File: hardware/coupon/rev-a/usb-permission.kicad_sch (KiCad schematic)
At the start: 31 parts, among them U10 SN74LVC1G00DBVR, U11 SN74LVC1G04DBVR, U12 SN74LVC1G04DBVR, U13 SN74LVC1G04DBVR, U14 SN74LVC1G04DBVR, U15 SN74LVC1G08DBVR, U16 SN74LVC1G32DBVR, U17 SN74LVC1G11DBVR, U18 SN74LVC1G08DBVR, U19 SN74LVC1G11DBVR, U20 SN74LVC1G11DBVR, U21 SN74LVC1G11DBVR, U22 SN74LVC1G32DBVR, U23 SN74LVC1G06DBVR

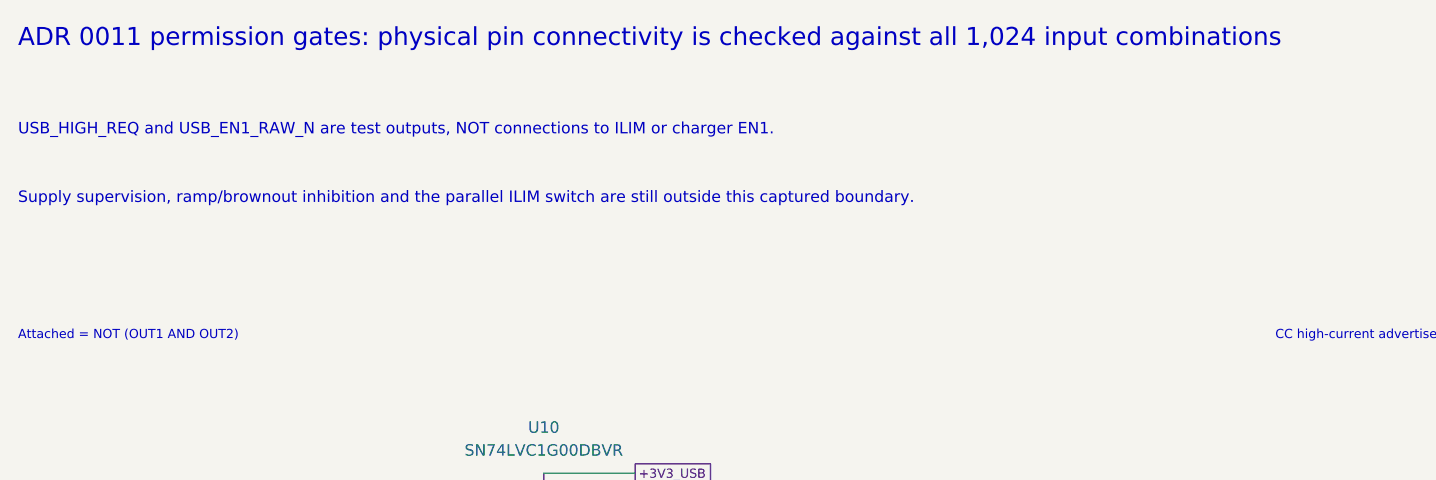
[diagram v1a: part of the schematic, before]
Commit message: Review native USB capture and add staged logic-rail supervision
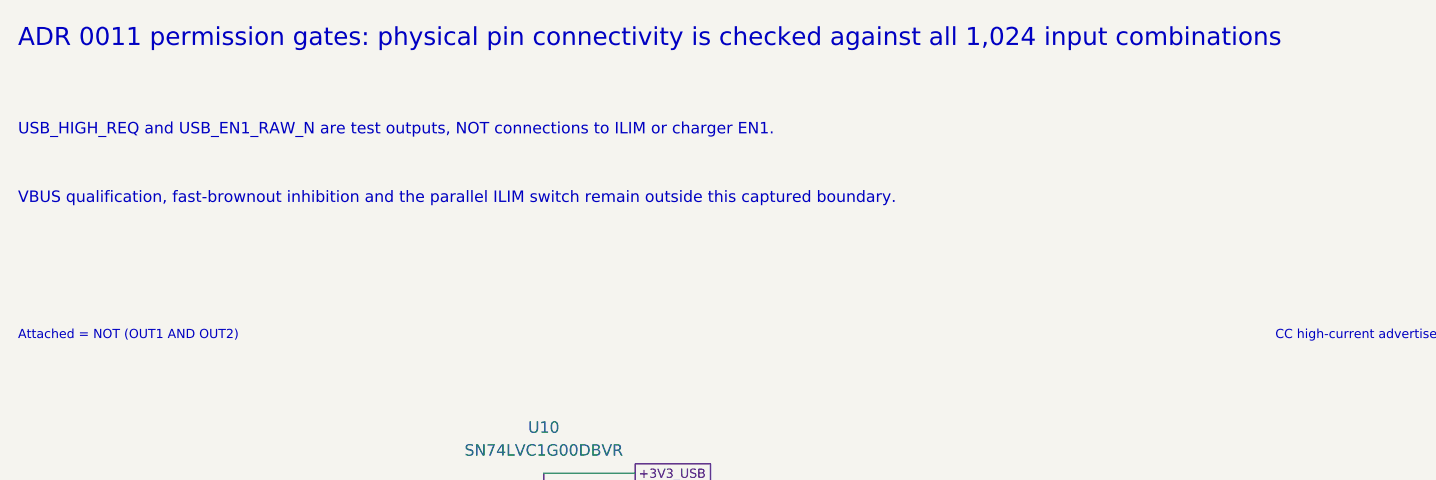
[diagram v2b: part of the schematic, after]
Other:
- note added: "VBUS qualification, fast-brownout inhibition and the parallel ILIM switch remain outside this captured boundary."
- note removed: "Supply supervision, ramp/brownout inhibition and the parallel ILIM switch are still outside this captured boundary."
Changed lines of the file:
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@@
 (text "ADR 0011 permission gates: physical pin connectivity is checked against all 1,024 input combinations" (at 20.320 20.320 0) (effects (font (size 2 2)) (justify left)))
 (text "USB_HIGH_REQ and USB_EN1_RAW_N are test outputs, NOT connections to ILIM or charger EN1." (at 20.320 30.480 0) (effects (font (size 1.27 1.27)) (justify left)))
-(text "Supply supervision, ramp/brownout inhibition and the parallel ILIM switch are still outside this captured boundary." (at 20.320 38.100 0) (effects (font (size 1.27 1.27)) (justify left)))
+(text "VBUS qualification, fast-brownout inhibition and the parallel ILIM switch remain outside this captured boundary." (at 20.320 38.100 0) (effects (font (size 1.27 1.27)) (justify left)))
 (text "Attached = NOT (OUT1 AND OUT2)" (at 20.320 53.340 0) (effects (font (size 1.016 1.016)) (justify left)))
 (symbol (lib_id "rgb-badge-coupon:SN74LVC1G00DBVR") (at 78.740 76.200 0) (unit 1)

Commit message: Simplify charging to Type-C-only fixed-current policy
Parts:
- removed C10, C12, C13, C14, C15, C16, C18, C19, C20, C21, C22: 100n 16V X7R, rgb-badge-coupon:C_Murata_GRM15_0402, symbol rgb-badge-coupon:GRM155R71C104KA88D
- removed U10: SN74LVC1G00DBVR, rgb-badge-coupon:SOT23_TI_DBV0005A, symbol rgb-badge-coupon:SN74LVC1G00DBVR
- removed U12, U13, U14: SN74LVC1G04DBVR, rgb-badge-coupon:SOT23_TI_DBV0005A, symbol rgb-badge-coupon:SN74LVC1G04DBVR
- removed U15, U18: SN74LVC1G08DBVR, rgb-badge-coupon:SOT23_TI_DBV0005A, symbol rgb-badge-coupon:SN74LVC1G08DBVR
- removed U16, U22: SN74LVC1G32DBVR, rgb-badge-coupon:SOT23_TI_DBV0005A, symbol rgb-badge-coupon:SN74LVC1G32DBVR
- removed U19, U20, U21: SN74LVC1G11DBVR, rgb-badge-coupon:SOT23_TI_DBV0006A, symbol rgb-badge-coupon:SN74LVC1G11DBVR
- TP30: value HIGH_REQ -> CHARGE_REQ
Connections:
- net USB_ATTACHED is gone; now on net USB_CC_HIGH: U17.6 (C)
- net USB_READY_ATTACHED is gone; now on net USB_CHARGE_REQ: U17.4 (Y)
- net USB_RUN_REQ is gone; now on net USB_CHARGE_REQ: U23.2 (A)
- net USB_HIGH_REQ renamed USB_CHARGE_REQ
- no-connect marks 5 -> 2
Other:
- note added: "ADR 0013: one fixed current limit; 16 stable Type-C/supply combinations checked"
- note added: "Both supplies valid AND Type-C permission"
- note added: "Open-drain request; not charger pin"
- note added: "Type-C advertises 1.5 A or 3 A"
- note added: "USB_CHARGE_REQ and USB_EN1_RAW_N are test outputs, NOT a physical charger EN1 connection."
- note added: "VBUS qualification and physical standby inhibition remain open. No switched ILIM branch."
- note removed: "ADR 0011 permission gates: physical pin connectivity is checked against all 1,024 input combinations"
- note removed: "Attached = NOT (OUT1 AND OUT2)"
- note removed: "BC data switch closed"
- note removed: "Both supplies valid AND attached"
- note removed: "CC high-current advertisement"
- note removed: "Either qualified route can request run"
- note removed: "Hardware source permission"
- note removed: "Hardware-only high-current request"
- note removed: "Low-current-only application route"
- note removed: "No charging-source flag"
- note removed: "ON AND running AND USB-stack grant"
- note removed: "Open-drain request output; not charger pin"
- note removed: "Positive BC classification"
- note removed: "Qualified BC high-current source"
- note removed: "SDP data-source qualification"
- note removed: "USB_HIGH_REQ and USB_EN1_RAW_N are test outputs, NOT connections to ILIM or charger EN1."
- note removed: "VBUS qualification, fast-brownout inhibition and the parallel ILIM switch remain outside this captured boundary."
- moved on the sheet: C11, C17, C23, U11, U17, U23

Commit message: Normalize Panasonic ERJ order codes across coupon
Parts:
- R70: symbol rgb-badge-coupon:ERJ-2RKF1002X -> rgb-badge-coupon:ERJ2RKF1002X; MPN ERJ-2RKF1002X -> ERJ2RKF1002X
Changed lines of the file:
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@@
 (wire (pts (xy 363.220 104.140) (xy 373.380 104.140)) (stroke (width 0) (type default)))
 (global_label "GND" (shape passive) (at 373.380 104.140 0) (effects (font (size 1.016 1.016)) (justify left)) (property "Intersheetrefs" "${INTERSHEET_REFS}" (at 373.380 104.140 0) (effects (font (size 1.27 1.27)) (hide yes))))
-(symbol (lib_id "rgb-badge-coupon:ERJ-2RKF1002X") (at 358.140 325.120 0) (unit 1)
+(symbol (lib_id "rgb-badge-coupon:ERJ2RKF1002X") (at 358.140 325.120 0) (unit 1)
 (exclude_from_sim no) (in_bom yes) (on_board yes) (dnp no)
 (property "Reference" "R70" (at 358.140 318.770 0) (effects (font (size 1.27 1.27))))
@@
 (property "Datasheet" "https://industrial.panasonic.com/cdbs/www-data/pdf/RDA0000/AOA0000C304.pdf" (at 358.140 325.120 0) (effects (font (size 1.27 1.27)) (hide yes)))
 (property "Manufacturer" "Panasonic" (at 358.140 325.120 0) (effects (font (size 1.27 1.27)) (hide yes)))
-(property "MPN" "ERJ-2RKF1002X" (at 358.140 325.120 0) (effects (font (size 1.27 1.27)) (hide yes)))
+(property "MPN" "ERJ2RKF1002X" (at 358.140 325.120 0) (effects (font (size 1.27 1.27)) (hide yes)))
 (pin "1")
 (pin "2")
